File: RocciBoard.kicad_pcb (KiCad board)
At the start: 2 copper layers, 99 x 54 mm, 195 parts, among them J1 Battery, J10 M3, J11 I2C6, J12 Power, J13 M2, J14 I2C7, J2 I2C0, J3 I2C1, J4 I2C2, J5 I2C3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

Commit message: finished #4 TODO list
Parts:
- moved C4 19.1 mm to (205.6, 86.5)
- moved C7 16.9 mm to (201.8, 105.1)
- moved R5 13.0 mm to (199.4, 104.1), turned to 0 degrees
- moved TP6 10.8 mm to (201.0, 96.7)
- moved R6 10.3 mm to (198.8, 95.9), turned to -90 degrees
- moved C2 9.28 mm to (203.6, 94.9)
- moved TP5 9.25 mm to (200.2, 103.3)
- moved C5 9.09 mm to (205.6, 91.5)
- moved U1 9.04 mm to (202.4, 99.5)
- moved C3 8.56 mm to (204.4, 104.3)
- moved C21 8.42 mm to (206.8, 94.9), turned to 180 degrees
- moved L1 7.32 mm to (207.6, 99.5), turned to 90 degrees
- moved R7 6.49 mm to (198.8, 101.5), turned to 90 degrees
- moved TP4 6.20 mm to (201.0, 94.5)
- moved TP1 6.20 mm to (203.2, 103.5)
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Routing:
- net +5V: track 262.3 -> 288.9 mm, vias 13 -> 16
- net /SW: track 9.17 -> 0.00 mm
- net /FB: track 12.1 -> 3.78 mm
- net Net-(U1-VCC): track 9.59 -> 14.7 mm, vias 1 -> 2
- net +12VA: track 173.8 -> 169.9 mm, vias 3 -> 7
- net /Boot: track 5.80 -> 2.48 mm
- net /PG: track 5.84 -> 3.11 mm
- net I2C_SDA: track 50.0 -> 52.5 mm
- net I2C_SCL: track 54.2 -> 55.9 mm
- net GND: vias 110 -> 103
- added copper zone on F.Cu, net +12VA
- added copper zone on F.Cu, net +5V
- added copper zone on F.Cu, net /SW

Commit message: lochraster ist fertig
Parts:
- moved TP7 30.0 mm to (139.3, 95.6)
- moved D26 8.78 mm to (174.8, 97.8), turned to -90 degrees
- moved J12 5.11 mm to (168.1, 90.4)
- moved F2 4.85 mm to (152.2, 88.3)
- moved F11 3.10 mm to (171.8, 98.1)
- moved D14 1.56 mm to (130.8, 120.3)
- moved R36 1.56 mm to (130.8, 123.4)
- moved D13 1.48 mm to (132.3, 120.3)
- moved R35 1.48 mm to (132.3, 123.4)
- moved G*** 1.03 mm to (147.6, 93.5)
- moved D32 0.66 mm to (173.9, 86.3), turned to 0 degrees
- moved C18 0.61 mm to (127.1, 118.0)
- moved C15 0.31 mm to (127.1, 125.9)
- moved C16 0.27 mm to (127.1, 110.3)
- turned D17 to 0 degrees
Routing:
- net +12V: track 130.0 -> 14.4 mm, vias 6 -> 37
- net +12VA: track 169.9 -> 148.5 mm, vias 7 -> 6
- net Net-(J12-Pin_2): track 6.76 -> 13.1 mm
- net +3V3: track 114.8 -> 120.3 mm
- net /12V_input: track 17.9 -> 12.6 mm
- net I2C_SDA: track 52.5 -> 53.4 mm
- net +5V: track 288.9 -> 289.6 mm
- net Net-(J12-Pin_3): track 4.73 -> 4.21 mm
- net GND: vias 103 -> 119
- added copper zone on B.Cu, net +12V
- added copper zone on F.Cu, net +12V
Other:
- board text added: "Battery"
- board text removed: "Akku"

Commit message: final version V1.0
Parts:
- moved U2 2.08 mm to (206.2, 114.0)
- moved U3 1.87 mm to (152.9, 100.0)
- moved C14 1.13 mm to (141.9, 99.3)
- moved D32 0.68 mm to (173.9, 85.6)
- moved F2 0.46 mm to (151.8, 88.3)
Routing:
- net +12V: track 14.4 -> 15.5 mm

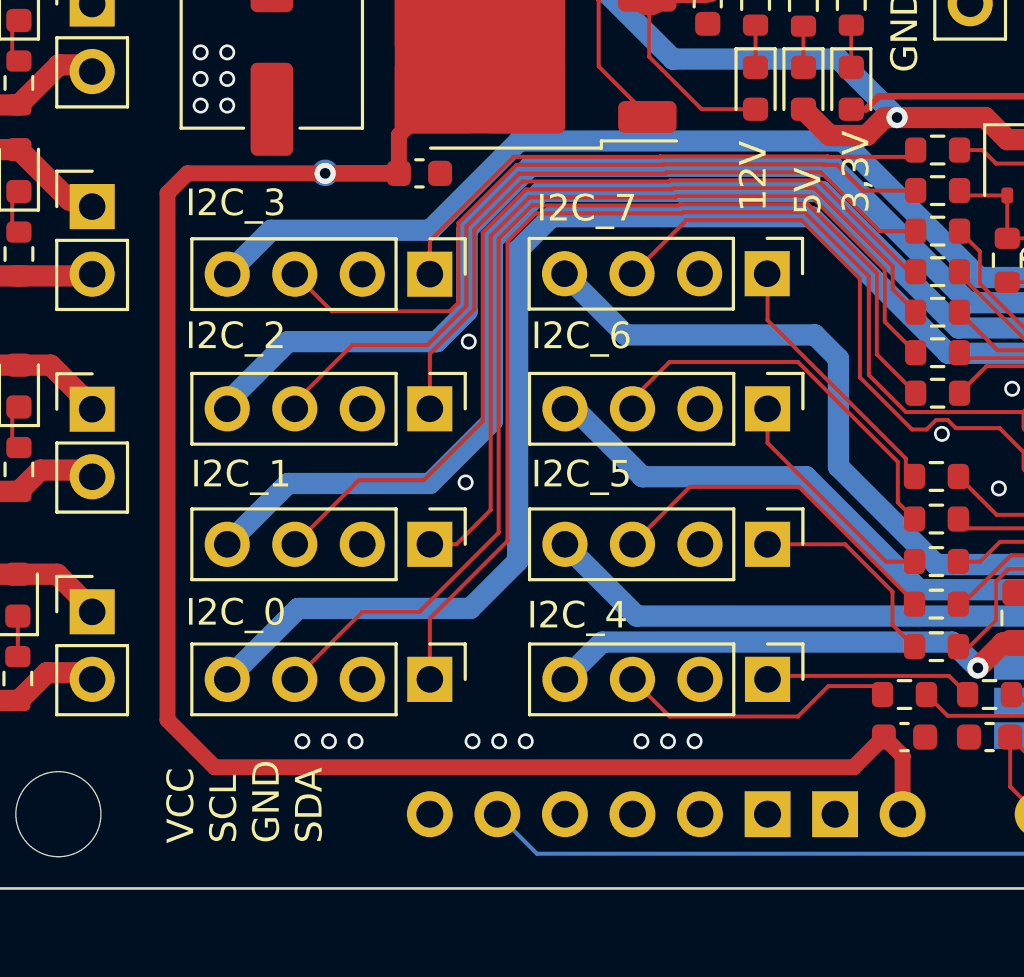
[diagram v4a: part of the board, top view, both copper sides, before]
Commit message: fix #8 prevent backcurrent from Arduino USB
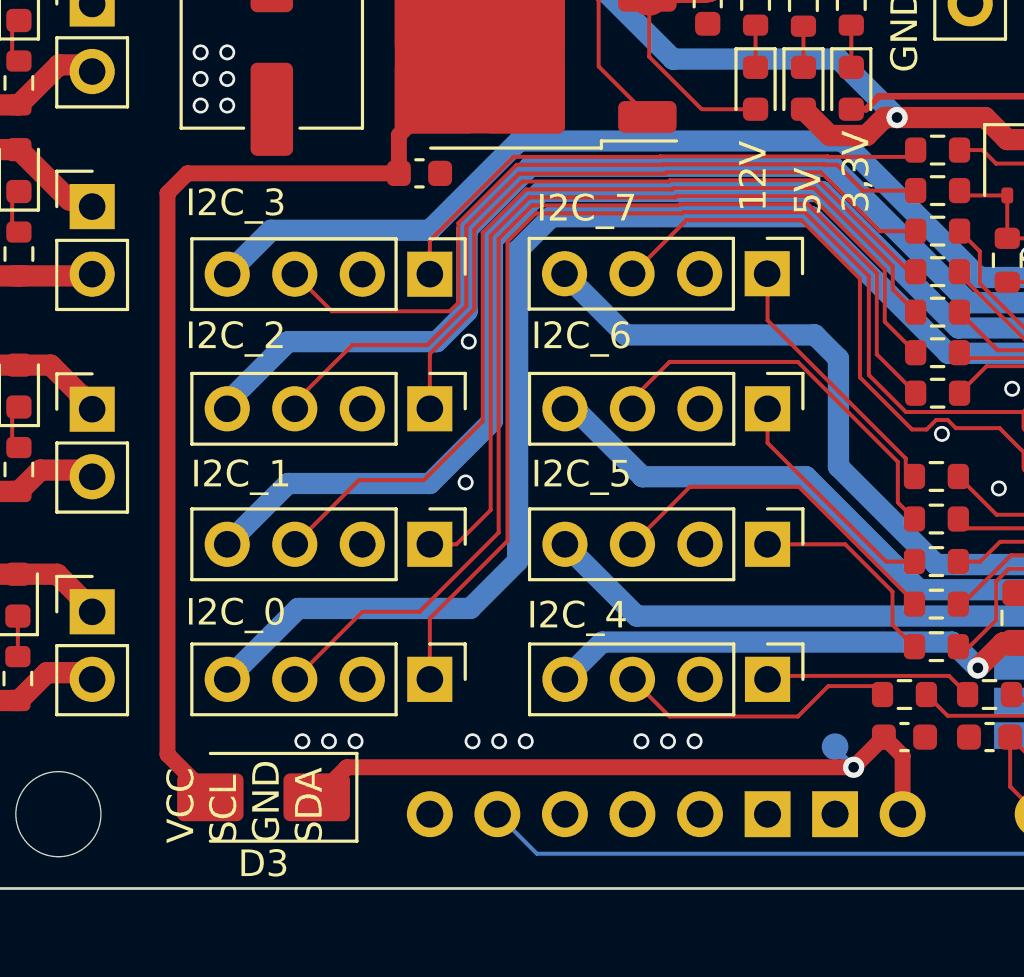
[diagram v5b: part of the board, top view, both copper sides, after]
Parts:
- removed TP12: ~, TestPoint:TestPoint_Pad_D1.0mm
- added D3: SS54, Diode_SMD:D_SMA, F.Cu at (141.6, 127.9)
- added TP23: ~, TestPoint:TestPoint_Pad_D1.0mm, B.Cu at (163.1, 126.0)
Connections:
- C13 pad 1: +8V -> /_8V
- R21 pad 2: +8V -> /_8V
- U3 pad 2: +8V -> /_8V
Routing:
- net +8V: track 69.3 -> 26.5 mm
- net /_8V: track 0.00 -> 38.8 mm

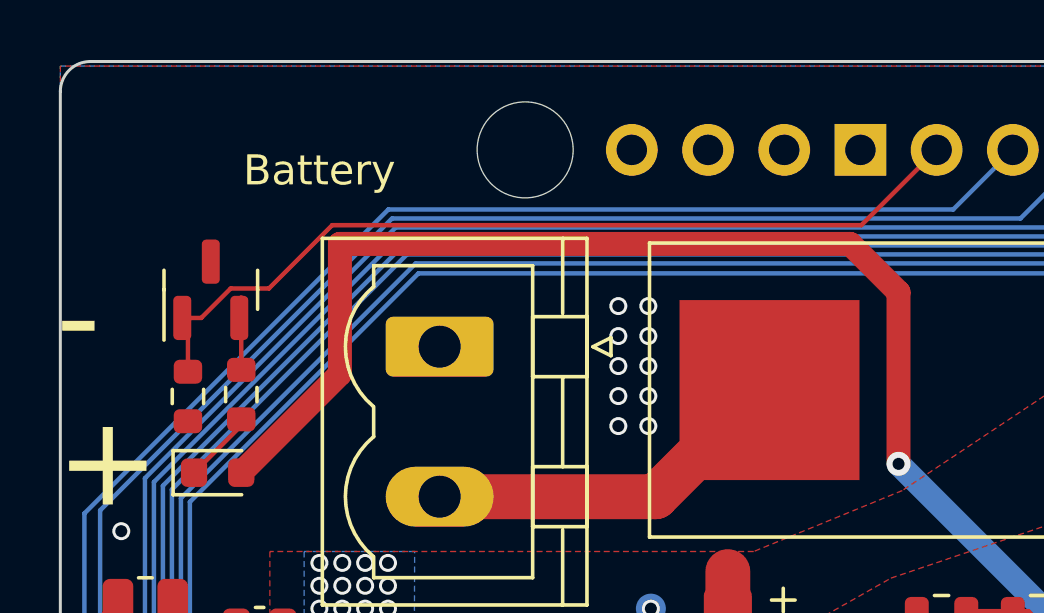
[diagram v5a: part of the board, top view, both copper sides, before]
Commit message: fix #5  Error LED Q2 Source<->Drain vertauscht
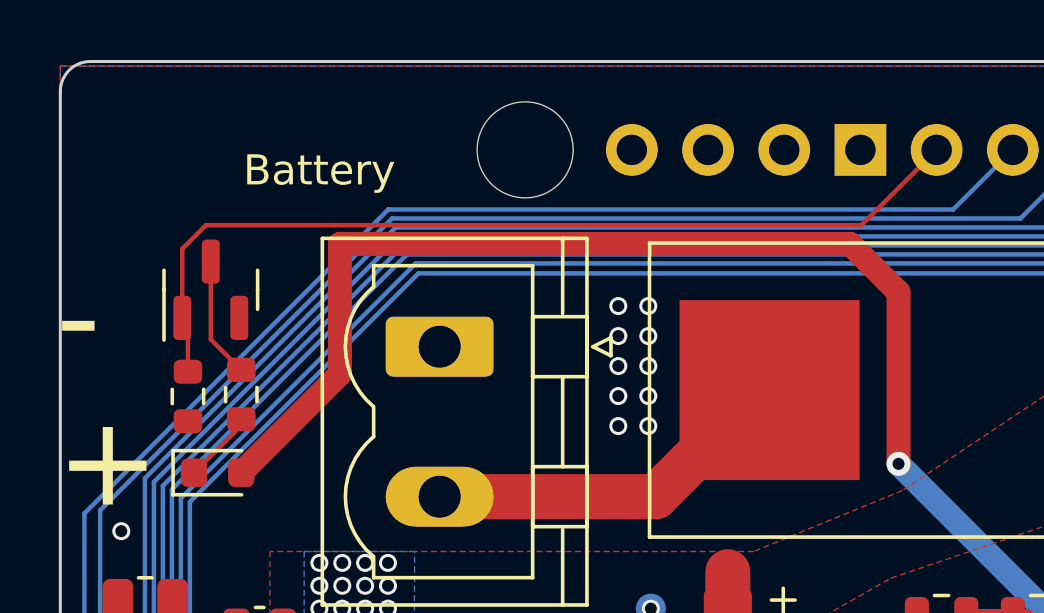
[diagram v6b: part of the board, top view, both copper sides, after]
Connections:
- Q2 pad 2: Net-(Q2-S) -> GND
- Q2 pad 3: GND -> Net-(Q2-D)
- R42 pad 2: Net-(Q2-S) -> Net-(Q2-D)
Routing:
- net Net-(Q2-D): track 0.00 -> 4.03 mm
- net Net-(Q2-S): track 2.03 -> 0.00 mm
- net ERROR_LED: track 29.3 -> 30.7 mm
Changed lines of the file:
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@@
   (net 152 "unconnected-(XA1-D3_INT1-PadD3)")
   (net 153 "unconnected-(XA1-D14{slash}TX3-PadD14)")
-  (net 154 "Net-(Q2-S)")
+  (net 154 "Net-(Q2-D)")
   (net 155 "Net-(U2-ADJ)")
   (net 156 "Net-(D28-K)")
@@
       (net 25 "Net-(D17-K)") (pintype "passive"))
     (pad "2" smd roundrect (at 0.825 0 90) (size 0.8 0.95) (layers "F.Cu" "F.Paste" "F.Mask") (roundrect_rratio 0.25)
-      (net 154 "Net-(Q2-S)") (pintype "passive"))
+      (net 154 "Net-(Q2-D)") (pintype "passive"))
     (model "${KICAD6_3DMODEL_DIR}/Resistor_SMD.3dshapes/R_0603_1608Metric.wrl"
       (offset (xyz 0 0 0))
@@
       (net 26 "ERROR_LED") (pinfunction "G") (pintype "input"))
     (pad "2" smd roundrect (at -0.9375 0.95 90) (size 1.475 0.6) (layers "F.Cu" "F.Paste" "F.Mask") (roundrect_rratio 0.25)
-      (net 154 "Net-(Q2-S)") (pinfunction "S") (pintype "passive"))
+      (net 2 "GND") (pinfunction "S") (pintype "passive"))
     (pad "3" smd roundrect (at 0.9375 0 90) (size 1.475 0.6) (layers "F.Cu" "F.Paste" "F.Mask") (roundrect_rratio 0.25)
-      (net 2 "GND") (pinfunction "D") (pintype "passive"))
+      (net 154 "Net-(Q2-D)") (pinfunction "D") (pintype "passive"))
     (model "${KICAD6_3DMODEL_DIR}/Package_TO_SOT_SMD.3dshapes/SOT-23.wrl"
       (offset (xyz 0 0 0))
@@
   (segment (start 124.0905 91.024) (end 125.6655 89.449) (width 0.15) (layer "F.Cu") (net 25))
   (segment (start 125.6655 89.449) (end 125.6655 89.246) (width 0.15) (layer "F.Cu") (net 25))
-  (segment (start 125.31517 84.882) (end 126.587 84.882) (width 0.15) (layer "F.Cu") (net 26))
+  (segment (start 123.6995 85.8655) (end 123.698 85.864) (width 0.15) (layer "F.Cu") (net 26))
+  (segment (start 123.698 85.864) (end 123.698 83.566) (width 0.15) (layer "F.Cu") (net 26))
+  (segment (start 124.49 82.774) (end 146.334 82.774) (width 0.15) (layer "F.Cu") (net 26))
   (segment (start 123.8875 87.659) (end 123.8875 86.0535) (width 0.15) (layer "F.Cu") (net 26))
-  (segment (start 146.334 82.774) (end 148.844 80.264) (width 0.15) (layer "F.Cu") (net 26))
-  (segment (start 124.33167 85.8655) (end 125.31517 84.882) (width 0.15) (layer "F.Cu") (net 26))
+  (segment (start 123.698 83.566) (end 124.49 82.774) (width 0.15) (layer "F.Cu") (net 26))
   (segment (start 123.8875 86.0535) (end 123.6995 85.8655) (width 0.15) (layer "F.Cu") (net 26))
-  (segment (start 123.6995 85.8655) (end 124.33167 85.8655) (width 0.15) (layer "F.Cu") (net 26))
-  (segment (start 126.587 84.882) (end 128.695 82.774) (width 0.15) (layer "F.Cu") (net 26))
-  (segment (start 128.695 82.774) (end 146.334 82.774) (width 0.15) (layer "F.Cu") (net 26))
+  (segment (start 146.334 82.774) (end 148.844 80.264) (width 0.15) (layer "F.Cu") (net 26))
   (segment (start 132.12 114.7355) (end 132.12 113.2115) (width 0.15) (layer "F.Cu") (net 27))
   (segment (start 130.596 114.7355) (end 130.596 113.2115) (width 0.15) (layer "F.Cu") (net 28))
@@
   (segment (start 197.358 79.681) (end 196.808 79.131) (width 0.15) (layer "B.Cu") (net 88))
   (segment (start 188.595 110.246) (end 191.389 110.246) (width 0.15) (layer "B.Cu") (net 88))
-  (segment (start 125.6655 85.182) (end 125.6655 87.214) (width 0.15) (layer "F.Cu") (net 154))
+  (segment (start 124.6495 86.58) (end 125.6655 87.596) (width 0.15) (layer "F.Cu") (net 154))
+  (segment (start 124.6495 83.9905) (end 124.6495 86.58) (width 0.15) (layer "F.Cu") (net 154))
   (segment (start 205.4475 117.124) (end 208.358 117.124) (width 0.15) (layer "F.Cu") (net 155))
   (segment (start 203.8275 118.744) (end 205.4475 117.124) (width 0.15) (layer "F.Cu") (net 155))

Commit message: fix #7 all status LEDs are too bright
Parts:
- R16, R35, R36, R43, R44, R51, R52, R58, R59: value 1k -> 2k
- R17: value 330 -> 620
- R18: value 150 -> 330
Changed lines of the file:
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@@
     (descr "Resistor SMD 0603 (1608 Metric), square (rectangular) end terminal, IPC_7351 nominal, (Body size source: IPC-SM-782 page 72, https://www.pcb-3d.com/wordpress/wp-content/uploads/ipc-sm-782a_amendment_1_and_2.pdf), generated with kicad-footprint-generator")
     (tags "resistor")
-    (property "LCSC" "C21190")
+    (property "LCSC" "C22975")
     (property "Sheetfile" "RocciBoard.kicad_sch")
     (property "Sheetname" "")
@@
         (effects (font (size 1 1) (thickness 0.15)))
     )
-    (fp_text value "1k" (at 0 1.43 90) (layer "F.Fab")
+    (fp_text value "2k" (at 0 1.43 90) (layer "F.Fab")
         (effects (font (size 1 1) (thickness 0.15)))
     )
@@
     (descr "Resistor SMD 0603 (1608 Metric), square (rectangular) end terminal, IPC_7351 nominal, (Body size source: IPC-SM-782 page 72, https://www.pcb-3d.com/wordpress/wp-content/uploads/ipc-sm-782a_amendment_1_and_2.pdf), generated with kicad-footprint-generator")
     (tags "resistor")
-    (property "LCSC" "C21190")
+    (property "LCSC" "C22975")
     (property "Sheetfile" "RocciBoard.kicad_sch")
     (property "Sheetname" "")
@@
         (effects (font (size 1 1) (thickness 0.15)))
     )
-    (fp_text value "1k" (at 0 1.43 90) (layer "F.Fab")
+    (fp_text value "2k" (at 0 1.43 90) (layer "F.Fab")
         (effects (font (size 1 1) (thickness 0.15)))
     )
@@
     (descr "Resistor SMD 0603 (1608 Metric), square (rectangular) end terminal, IPC_7351 nominal, (Body size source: IPC-SM-782 page 72, https://www.pcb-3d.com/wordpress/wp-content/uploads/ipc-sm-782a_amendment_1_and_2.pdf), generated with kicad-footprint-generator")
     (tags "resistor")
-    (property "LCSC" "C21190")
+    (property "LCSC" "C22975")
     (property "Sheetfile" "RocciBoard.kicad_sch")
     (property "Sheetname" "")
@@
         (effects (font (size 1 1) (thickness 0.15)))
     )
-    (fp_text value "1k" (at 0 1.43 90) (layer "F.Fab")
+    (fp_text value "2k" (at 0 1.43 90) (layer "F.Fab")
         (effects (font (size 1 1) (thickness 0.15)))
     )
@@
     (descr "Resistor SMD 0603 (1608 Metric), square (rectangular) end terminal, IPC_7351 nominal, (Body size source: IPC-SM-782 page 72, https://www.pcb-3d.com/wordpress/wp-content/uploads/ipc-sm-782a_amendment_1_and_2.pdf), generated with kicad-footprint-generator")
     (tags "resistor")
-    (property "LCSC" "C21190")
+    (property "LCSC" "C22975")
     (property "Sheetfile" "RocciBoard.kicad_sch")
     (property "Sheetname" "")
@@
         (effects (font (size 1 1) (thickness 0.15)))
     )
-    (fp_text value "1k" (at 0 1.43 90) (layer "F.Fab")
+    (fp_text value "2k" (at 0 1.43 90) (layer "F.Fab")
         (effects (font (size 1 1) (thickness 0.15)))
     )
@@
     (descr "Resistor SMD 0603 (1608 Metric), square (rectangular) end terminal, IPC_7351 nominal, (Body size source: IPC-SM-782 page 72, https://www.pcb-3d.com/wordpress/wp-content/uploads/ipc-sm-782a_amendment_1_and_2.pdf), generated with kicad-footprint-generator")
     (tags "resistor")
-    (property "LCSC" "C21190")
+    (property "LCSC" "C22975")
     (property "Sheetfile" "RocciBoard.kicad_sch")
     (property "Sheetname" "")
@@
         (effects (font (size 1 1) (thickness 0.15)))
     )
-    (fp_text value "1k" (at 0 1.43 90) (layer "F.Fab")
+    (fp_text value "2k" (at 0 1.43 90) (layer "F.Fab")
         (effects (font (size 1 1) (thickness 0.15)))
     )
@@
     (descr "Resistor SMD 0603 (1608 Metric), square (rectangular) end terminal, IPC_7351 nominal, (Body size source: IPC-SM-782 page 72, https://www.pcb-3d.com/wordpress/wp-content/uploads/ipc-sm-782a_amendment_1_and_2.pdf), generated with kicad-footprint-generator")
     (tags "resistor")
-    (property "LCSC" "C21190")
+    (property "LCSC" "C22975")
     (property "Sheetfile" "RocciBoard.kicad_sch")
     (property "Sheetname" "")
@@
         (effects (font (size 1 1) (thickness 0.15)))
     )
-    (fp_text value "1k" (at 0 1.43 90) (layer "F.Fab")
+    (fp_text value "2k" (at 0 1.43 90) (layer "F.Fab")
         (effects (font (size 1 1) (thickness 0.15)))
     )
@@
     (descr "Resistor SMD 0603 (1608 Metric), square (rectangular) end terminal, IPC_7351 nominal, (Body size source: IPC-SM-782 page 72, https://www.pcb-3d.com/wordpress/wp-content/uploads/ipc-sm-782a_amendment_1_and_2.pdf), generated with kicad-footprint-generator")
     (tags "resistor")
-    (property "LCSC" "C21190")
+    (property "LCSC" "C22975")
     (property "Sheetfile" "RocciBoard.kicad_sch")
     (property "Sheetname" "")
@@
         (effects (font (size 1 1) (thickness 0.15)))
     )
-    (fp_text value "1k" (at 0 1.43 90) (layer "F.Fab")
+    (fp_text value "2k" (at 0 1.43 90) (layer "F.Fab")
         (effects (font (size 1 1) (thickness 0.15)))
     )
@@
     (descr "Resistor SMD 0603 (1608 Metric), square (rectangular) end terminal, IPC_7351 nominal, (Body size source: IPC-SM-782 page 72, https://www.pcb-3d.com/wordpress/wp-content/uploads/ipc-sm-782a_amendment_1_and_2.pdf), generated with kicad-footprint-generator")
     (tags "resistor")
-    (property "LCSC" "C22808")
+    (property "LCSC" "C23138")
     (property "Sheetfile" "RocciBoard.kicad_sch")
     (property "Sheetname" "")
@@
         (effects (font (size 1 1) (thickness 0.15)))
     )
-    (fp_text value "150" (at 0 1.43 90) (layer "F.Fab")
+    (fp_text value "330" (at 0 1.43 90) (layer "F.Fab")
         (effects (font (size 1 1) (thickness 0.15)))
     )
@@
     (descr "Resistor SMD 0603 (1608 Metric), square (rectangular) end terminal, IPC_7351 nominal, (Body size source: IPC-SM-782 page 72, https://www.pcb-3d.com/wordpress/wp-content/uploads/ipc-sm-782a_amendment_1_and_2.pdf), generated with kicad-footprint-generator")
     (tags "resistor")
-    (property "LCSC" "C23138")
+    (property "LCSC" "C23228")
     (property "Sheetfile" "RocciBoard.kicad_sch")
     (property "Sheetname" "")
@@
         (effects (font (size 1 1) (thickness 0.15)))
     )
-    (fp_text value "330" (at 0 1.43 90) (layer "F.Fab")
+    (fp_text value "620" (at 0 1.43 90) (layer "F.Fab")
         (effects (font (size 1 1) (thickness 0.15)))
     )
@@
     (descr "Resistor SMD 0603 (1608 Metric), square (rectangular) end terminal, IPC_7351 nominal, (Body size source: IPC-SM-782 page 72, https://www.pcb-3d.com/wordpress/wp-content/uploads/ipc-sm-782a_amendment_1_and_2.pdf), generated with kicad-footprint-generator")
     (tags "resistor")
-    (property "LCSC" "C21190")
+    (property "LCSC" "C22975")
     (property "Sheetfile" "RocciBoard.kicad_sch")
     (property "Sheetname" "")
@@
         (effects (font (size 1 1) (thickness 0.15)))
     )
-    (fp_text value "1k" (at 0 1.43 90) (layer "F.Fab")
+    (fp_text value "2k" (at 0 1.43 90) (layer "F.Fab")
         (effects (font (size 1 1) (thickness 0.15)))
     )
@@
     (descr "Resistor SMD 0603 (1608 Metric), square (rectangular) end terminal, IPC_7351 nominal, (Body size source: IPC-SM-782 page 72, https://www.pcb-3d.com/wordpress/wp-content/uploads/ipc-sm-782a_amendment_1_and_2.pdf), generated with kicad-footprint-generator")
     (tags "resistor")
-    (property "LCSC" "C21190")
+    (property "LCSC" "C22975")
     (property "Sheetfile" "RocciBoard.kicad_sch")
     (property "Sheetname" "")
@@
         (effects (font (size 1 1) (thickness 0.15)))
     )
-    (fp_text value "1k" (at 0 1.43 90) (layer "F.Fab")
+    (fp_text value "2k" (at 0 1.43 90) (layer "F.Fab")
         (effects (font (size 1 1) (thickness 0.15)))
     )
